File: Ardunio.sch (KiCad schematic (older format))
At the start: 11 parts, among them J2 Conn_01x06, J3 ISP, U6 ATMEGA328-AU, Y1 Crystal_GND2

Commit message: updated design
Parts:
- removed U6: ATMEGA328-AU, Housings_QFP:TQFP-32_7x7mm_Pitch0.8mm, symbol atmel:ATMEGA328-AU
- added U?: ATMEGA328-AU, Package_QFP:TQFP-32_7x7mm_P0.8mm, symbol MCU_Atmel_ATMEGA:ATMEGA328-AU
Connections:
- net +3V3: now also U?.18 (AVCC), U?.4 (VCC), U?.6 (VCC)
- net A0: now also U?.23 ((PCINT8/ADC0)PC0)
- net A1: now also U?.24 ((PCINT9/ADC1)PC1)
- net A2: now also U?.25 ((PCINT10/ADC2)PC2)
- net A3: now also U?.26 ((PCINT11/ADC3)PC3)
- net A6: now also U?.19 (ADC6)
- net A7: now also U?.22 (ADC7)
- net D10: now also U?.14 ((PCINT2/OC1B/~SS~)PB2)
- net D2: now also U?.32 ((PCINT18/INT0)PD2)
- net D3: now also U?.1 ((PCINT19/OC2B/INT1)PD3)
- net D4: now also U?.2 ((PCINT20/XCK/T0)PD4)
- net D5: now also U?.9 ((PCINT21/OC0B/T1)PD5)
- net D6: now also U?.10 ((PCINT22/OC0A/AIN0)PD6)
- net D7: now also U?.11 ((PCINT23/AIN1)PD7)
- net D8: now also U?.12 ((PCINT0/CLKO/ICP1)PB0)
- net D9: now also U?.13 ((PCINT1/OC1A)PB1)
- net GND: now also U?.21 (GND), U?.3 (GND), U?.5 (GND)
- net MISO: now also U?.16 ((PCINT4/MISO)PB4)
- net MOSI: now also U?.15 ((PCINT3/OC2A/MOSI)PB3)
- net RESET: now also U?.29 ((PCINT14/~RESET~)PC6)
- net RX1: now also U?.30 ((PCINT16/RXD)PD0)
- net SCK: now also U?.17 ((PCINT5/SCK)PB5)
- net SCL: now also U?.28 ((PCINT13/SCL/ADC5)PC5)
- net SDA: now also U?.27 ((PCINT12/SDA/ADC4)PC4)
- net TX0: now also U?.31 ((PCINT17/TXD)PD1)
- net at C9.1: now also U?.20 (AREF)
- net at Y1.3: now also U?.7 ((PCINT6/XTAL1/TOSC1)PB6)
- net at Y1.1: now also U?.8 ((PCINT7/XTAL2/TOSC2)PB7)
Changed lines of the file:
@@
 $EndComp
 $Comp
-L atmel:ATMEGA328-AU U6
-U 1 1 5B11F80F
+L MCU_Atmel_ATMEGA:ATMEGA328-AU U?
+U 1 1 5B216C7D
 P 4750 3150
-F 0 "U6" H 4800 4517 50  0000 C CNN
+F 0 "U?" H 4800 4517 50  0000 C CNN
 F 1 "ATMEGA328-AU" H 4800 4426 50  0000 C CNN
-F 2 "Housings_QFP:TQFP-32_7x7mm_Pitch0.8mm" H 4750 3150 50  0001 C CIN
-F 3 "http://www.atmel.com/images/atmel-8271-8-bit-avr-microcontroller-atmega48a-48pa-88a-88pa-168a-168pa-328-328p_datasheet.pdf" H 4750 3150 50  0001 C CNN
+F 2 "Package_QFP:TQFP-32_7x7mm_P0.8mm" H 4750 3150 50  0001 C CIN
+F 3 "http://ww1.microchip.com/downloads/en/DeviceDoc/atmel-8271-8-bit-avr-microcontroller-atmega48a-48pa-88a-88pa-168a-168pa-328-328p_datasheet.pdf" H 4750 3150 50  0001 C CNN
 	1    4750 3150
 	1    0    0    -1

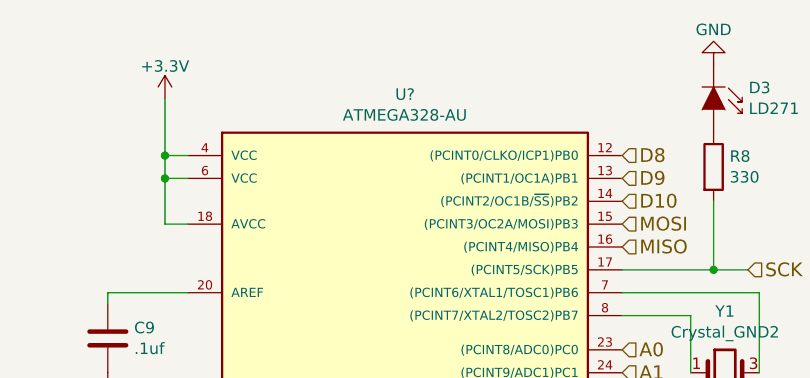
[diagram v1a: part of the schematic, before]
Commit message: added SD card
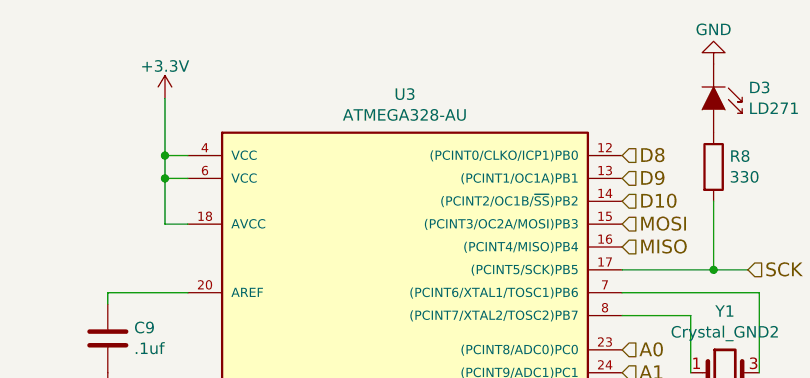
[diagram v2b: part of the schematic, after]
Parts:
- gave numbers to parts that had none: 1
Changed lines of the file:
@@
 $EndComp
 $Comp
-L MCU_Atmel_ATMEGA:ATMEGA328-AU U?
+L MCU_Atmel_ATMEGA:ATMEGA328-AU U3
 U 1 1 5B216C7D
 P 4750 3150
-F 0 "U?" H 4800 4517 50  0000 C CNN
+F 0 "U3" H 4800 4517 50  0000 C CNN
 F 1 "ATMEGA328-AU" H 4800 4426 50  0000 C CNN
 F 2 "Package_QFP:TQFP-32_7x7mm_P0.8mm" H 4750 3150 50  0001 C CIN

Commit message: flipped screen
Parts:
- J3: symbol Connector_Generic:Conn_02x03_Top_Bottom -> Connector_Generic:Conn_02x03_Odd_Even
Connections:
- net MOSI: now also J3.4 (Pin_4); no longer J3.5 (Pin_5)
- net RESET: now also J3.5 (Pin_5); no longer J3.3 (Pin_3)
- net SCK: now also J3.3 (Pin_3); no longer J3.2 (Pin_2)
- net VCC: now also J3.2 (Pin_2); no longer J3.4 (Pin_4)
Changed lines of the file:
@@
 $EndComp
 $Comp
-L Connector_Generic:Conn_02x03_Top_Bottom J3
+L Connector_Generic:Conn_02x03_Odd_Even J3
 U 1 1 5B121CDB
 P 8250 1900
